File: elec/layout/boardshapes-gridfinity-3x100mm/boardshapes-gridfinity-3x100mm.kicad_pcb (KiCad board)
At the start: 6 copper layers, 122 x 100 mm, 0 parts

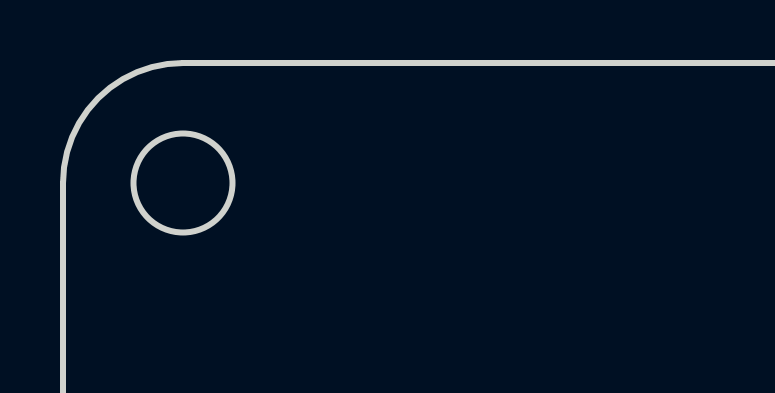
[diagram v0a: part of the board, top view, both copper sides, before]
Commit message: Attach nets to zones on template board
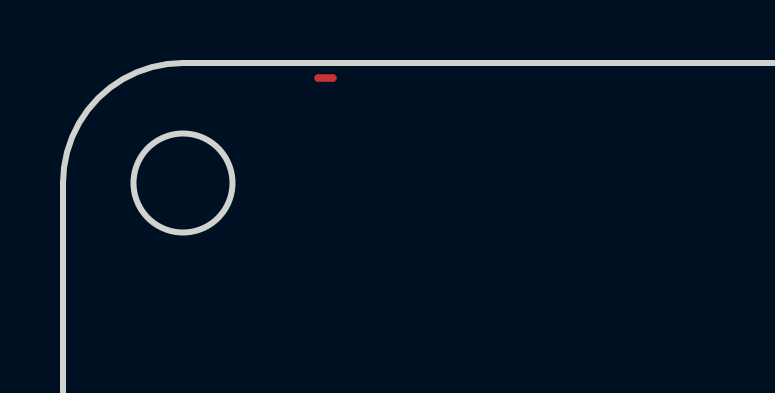
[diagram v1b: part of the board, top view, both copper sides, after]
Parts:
- added R1: , lib:NetTie-2_SMD_Pad0.25mm, F.Cu at (94.0, 43.5)
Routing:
- added copper zone on B.Cu, net GND
- added copper zone on F.Cu, net GND
- added copper zone on In1.Cu, net GND
- added copper zone on In4.Cu, net POWER_24V
- added copper zone on In2.Cu, net POWER_3V3
- added copper zone on In3.Cu, net POWER_5V
- removed copper zone on B.Cu, net (none)
- removed copper zone on F.Cu, net (none)
- removed copper zone on In1.Cu, net (none)
- removed copper zone on In2.Cu, net (none)
- removed copper zone on In3.Cu, net (none)
- removed copper zone on In4.Cu, net (none)
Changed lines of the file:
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@@
 	)
 	(net 0 "")
+	(net 1 "handle-net-1")
+	(net 2 "handle-net")
+	(net 3 "POWER_24V")
+	(net 4 "POWER_5V")
+	(net 5 "POWER_3V3")
+	(net 6 "GND")
+	(footprint "lib:NetTie-2_SMD_Pad0.25mm"
+		(layer "F.Cu")
+		(at 94 43.5)
+		(property "Reference" "R1"
+			(at 0 -1.2 0)
+			(layer "F.SilkS")
+			(hide yes)
+			(effects
+				(font
+					(size 1 1)
+					(thickness 0.15)
+				)
+			)
+		)
+		(property "Value" ""
+			(at 0 1.2 0)
+			(layer "F.Fab")
+			(effects
+				(font
+					(size 1 1)
+					(thickness 0.15)
+				)
+			)
+		)
+		(property "Datasheet" ""
+			(at 0 0 0)
+			(layer "F.Fab")
+			(hide yes)
+			(effects
+				(font
+					(size 1.27 1.27)
+					(thickness 0.15)
+				)
+			)
+		)
+		(property "Description" ""
+			(at 0 0 0)
+			(layer "F.Fab")
+			(hide yes)
+			(effects
+				(font
+					(size 1.27 1.27)
+					(thickness 0.15)
+				)
+			)
+		)
+		(property "__atopile_lib_fp_hash__" "04339b4f-90b8-45a9-eed6-f97325ef4d8a"
+			(at 0 0 0)
+			(layer "User.9")
+			(hide yes)
+			(effects
+				(font
+					(size 0.125 0.125)
+					(thickness 0.01875)
+				)
+			)
+		)
+		(property "LCSC" "C25744"
+			(at 0 0 0)
+			(layer "User.9")
+			(hide yes)
+			(effects
+				(font
+					(size 0.125 0.125)
+					(thickness 0.01875)
+				)
+			)
+		)
+		(property "Partnumber" "NetTie_250u"
+			(at 0 0 0)
+			(layer "User.9")
+			(hide yes)
+			(effects
+				(font
+					(size 0.125 0.125)
+					(thickness 0.01875)
+				)
+			)
+		)
+		(property "Manufacturer" "UNI-ROYAL(Uniroyal Elec)"
+			(at 0 0 0)
+			(layer "User.9")
+			(hide yes)
+			(effects
+				(font
+					(size 0.125 0.125)
+					(thickness 0.01875)
+				)
+			)
+		)
+		(property "JLCPCB description" "62.5mW Thick Film Resistors 50V ±100ppm/℃ ±1% 10kΩ 0402 Chip Resistor - Surface Mount ROHS"
+			(at 0 0 0)
+			(layer "User.9")
+			(hide yes)
+			(effects
+				(font
+					(size 0.125 0.125)
+					(thickness 0.01875)
+				)
+			)
+		)
+		(property "atopile_address" "handle"
+			(at 0 0 0)
+			(layer "User.9")
+			(hide yes)
+			(effects
+				(font
+					(size 0.125 0.125)
+					(thickness 0.01875)
+				)
+			)
+		)
+		(attr exclude_from_pos_files exclude_from_bom)
+		(fp_poly
+			(pts
+				(xy 0 -0.125) (xy 0.5 -0.125) (xy 0.5 0.125) (xy 0 0.125)
+			)
+			(stroke
+				(width 0)
+				(type solid)
+			)
+			(fill yes)
+			(layer "F.Cu")
+		)
+		(pad "1" smd circle
+			(at 0 0)
+			(size 0.25 0.25)
+			(layers "F.Cu")
+			(net 1 "handle-net-1")
+		)
+		(pad "2" smd circle
+			(at 0.5 0)
+			(size 0.25 0.25)
+			(layers "F.Cu")
+			(net 2 "handle-net")
+		)
+		(embedded_fonts no)
+	)
 	(gr_circle
 		(center 203.5 47)
@@
 	)
 	(zone
-		(net 0)
-		(net_name "")
+		(net 6)
+		(net_name "GND")
 		(layers "F.Cu" "B.Cu" "In1.Cu")
 		(name "gnd")
@@
 	)
 	(zone
-		(net 0)
-		(net_name "")
+		(net 5)
+		(net_name "POWER_3V3")
 		(layer "In2.Cu")
 		(name "3v3")
@@
 	)
 	(zone
-		(net 0)
-		(net_name "")
+		(net 4)
+		(net_name "POWER_5V")
 		(layer "In3.Cu")
 		(name "5v")
@@
 	)
 	(zone
-		(net 0)
-		(net_name "")
+		(net 3)
+		(net_name "POWER_24V")
 		(layer "In4.Cu")
 		(name "24v")

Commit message: fix board shape, update CAN termination
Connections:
- R1 pad 1: handle-net-1 -> handle-net
- R1 pad 2: handle-net -> handle-net-1
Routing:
- added copper zone on B.Cu, net (none)
- added copper zone on F.Cu, net (none)
- added copper zone on In1.Cu, net (none)
- added copper zone on In2.Cu, net (none)
- added copper zone on In3.Cu, net (none)
- added copper zone on In4.Cu, net (none)
- removed copper zone on B.Cu, net GND
- removed copper zone on F.Cu, net GND
- removed copper zone on In1.Cu, net GND
- removed copper zone on In4.Cu, net POWER_24V
- removed copper zone on In2.Cu, net POWER_3V3
- removed copper zone on In3.Cu, net POWER_5V
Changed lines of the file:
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@@
 	)
 	(net 0 "")
-	(net 1 "handle-net-1")
-	(net 2 "handle-net")
-	(net 3 "POWER_24V")
-	(net 4 "POWER_5V")
-	(net 5 "POWER_3V3")
-	(net 6 "GND")
+	(net 1 "handle-net")
+	(net 2 "handle-net-1")
 	(footprint "lib:NetTie-2_SMD_Pad0.25mm"
 		(layer "F.Cu")
@@
 			(size 0.25 0.25)
 			(layers "F.Cu")
-			(net 1 "handle-net-1")
+			(net 1 "handle-net")
 		)
 		(pad "2" smd circle
@@
 			(size 0.25 0.25)
 			(layers "F.Cu")
-			(net 2 "handle-net")
+			(net 2 "handle-net-1")
 		)
 		(embedded_fonts no)
@@
 	)
 	(zone
-		(net 6)
-		(net_name "GND")
+		(net 0)
+		(net_name "")
 		(layers "F.Cu" "B.Cu" "In1.Cu")
 		(name "gnd")
@@
 	)
 	(zone
-		(net 5)
-		(net_name "POWER_3V3")
+		(net 0)
+		(net_name "")
 		(layer "In2.Cu")
 		(name "3v3")
@@
 	)
 	(zone
-		(net 4)
-		(net_name "POWER_5V")
+		(net 0)
+		(net_name "")
 		(layer "In3.Cu")
 		(name "5v")
@@
 	)
 	(zone
-		(net 3)
-		(net_name "POWER_24V")
+		(net 0)
+		(net_name "")
 		(layer "In4.Cu")
 		(name "24v")

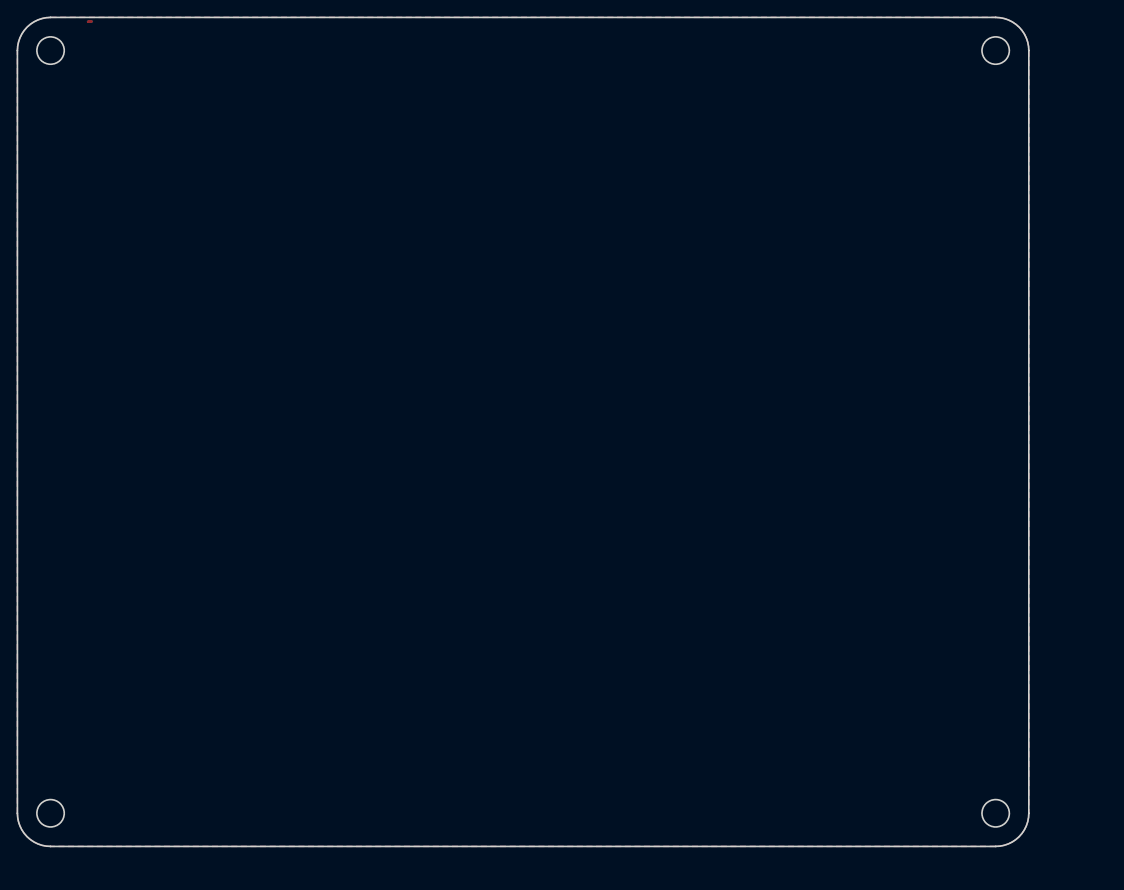
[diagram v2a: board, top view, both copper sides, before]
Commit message: Fix board shapes and CAN termination
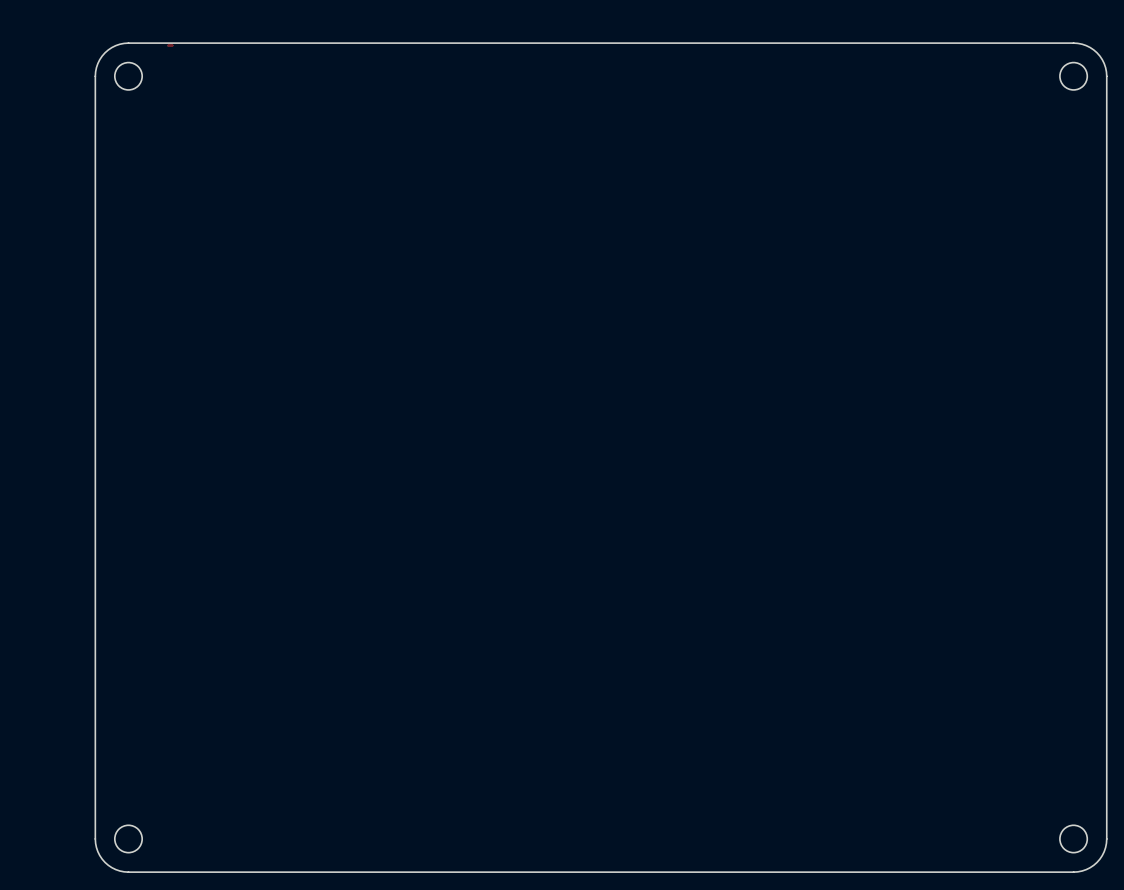
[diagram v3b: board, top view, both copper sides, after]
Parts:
- removed R1: , lib:NetTie-2_SMD_Pad0.25mm
- added U1: , lib:NetTie-2_SMD_Pad0.25mm, F.Cu at (103.7, 46.4)
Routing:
- removed copper zone on B.Cu, net (none)
- removed copper zone on F.Cu, net (none)
- removed copper zone on In1.Cu, net (none)
- removed copper zone on In2.Cu, net (none)
- removed copper zone on In3.Cu, net (none)
- removed copper zone on In4.Cu, net (none)
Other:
- outline, holes or cut-outs redrawn
- copper layers 6 -> 2

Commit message: checkin
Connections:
- U1 pad 1: handle-net-1 -> handle-net
- U1 pad 2: handle-net -> handle-net-1
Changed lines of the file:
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@@
     )
     (net 0 "")
-    (net 1 "handle-net-1")
-    (net 2 "handle-net")
+    (net 1 "handle-net")
+    (net 2 "handle-net-1")
     (footprint "lib:NetTie-2_SMD_Pad0.25mm"
         (layer "F.Cu")
@@
             (size 0.25 0.25)
             (layers "F.Cu")
-            (net 1 "handle-net-1")
+            (net 1 "handle-net")
         )
         (pad "2" smd circle
@@
             (size 0.25 0.25)
             (layers "F.Cu")
-            (net 2 "handle-net")
+            (net 2 "handle-net-1")
         )
         (embedded_fonts no)

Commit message: build with excluded checks
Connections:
- U1 pad 1: handle-net -> handle-net-1
- U1 pad 2: handle-net-1 -> handle-net
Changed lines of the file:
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@@
     )
     (net 0 "")
-    (net 1 "handle-net")
-    (net 2 "handle-net-1")
+    (net 1 "handle-net-1")
+    (net 2 "handle-net")
     (footprint "lib:NetTie-2_SMD_Pad0.25mm"
         (layer "F.Cu")
@@
             (size 0.25 0.25)
             (layers "F.Cu")
-            (net 1 "handle-net")
+            (net 1 "handle-net-1")
         )
         (pad "2" smd circle
@@
             (size 0.25 0.25)
             (layers "F.Cu")
-            (net 2 "handle-net-1")
+            (net 2 "handle-net")
         )
         (embedded_fonts no)
